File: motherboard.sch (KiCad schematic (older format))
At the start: 90 parts, among them P1 CONN_01X08, P2 CONN_01X08, P3 CONN_01X29, P4 CONN_01X25, U1 STM32F411-LQFP64, U10 74LS125, U11 74LS125, U12 74LS125, U13 74LS125, U14 74LS125, U15 PCA9517A, U16 PCA9517A, U2 STM32F411-LQFP64, U3 AP7313, U4 74LVC2G132, U5 FM25V20A-G, U6 FM25V20A-G, U7 FM25V20A-G, U8 FM25V20A-G, U9 74LS125, Y1 32k, Y2 8M(16pF), Y3 32k, Y4 8M(16pF)

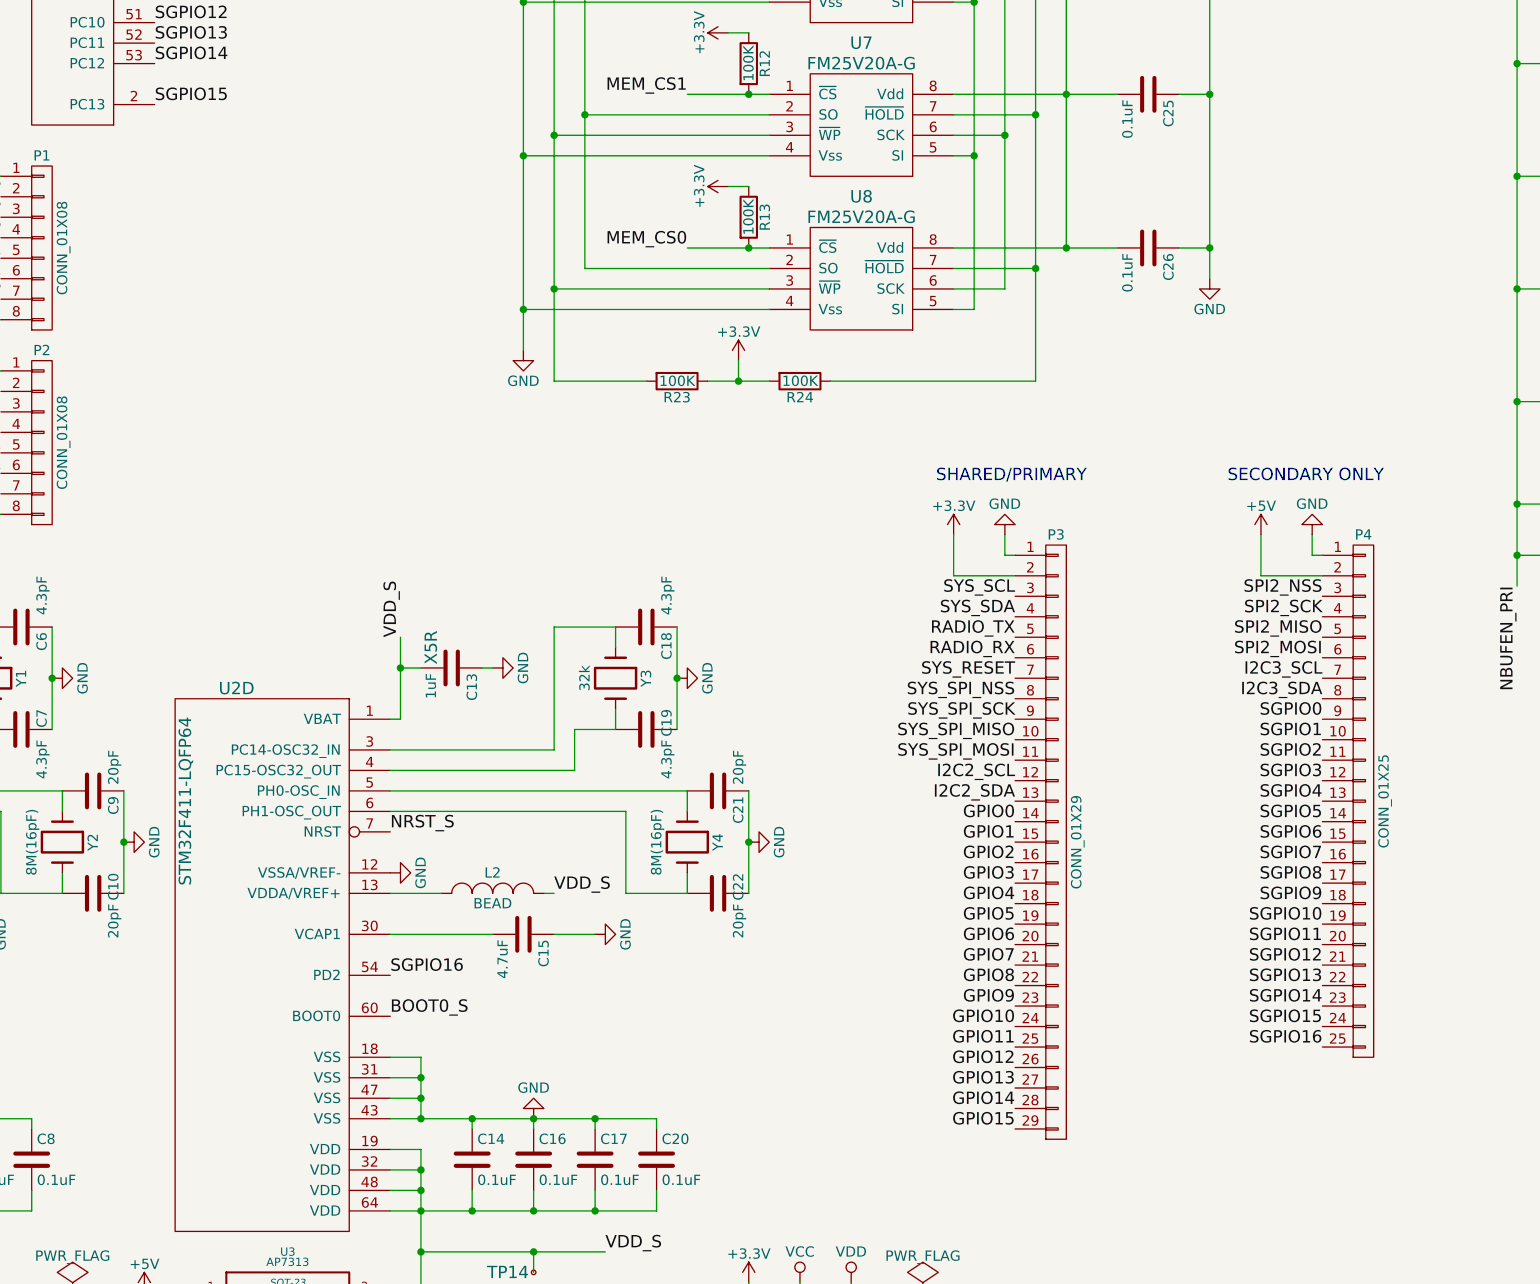
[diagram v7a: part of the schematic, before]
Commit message: Began adding real connectors to schematic
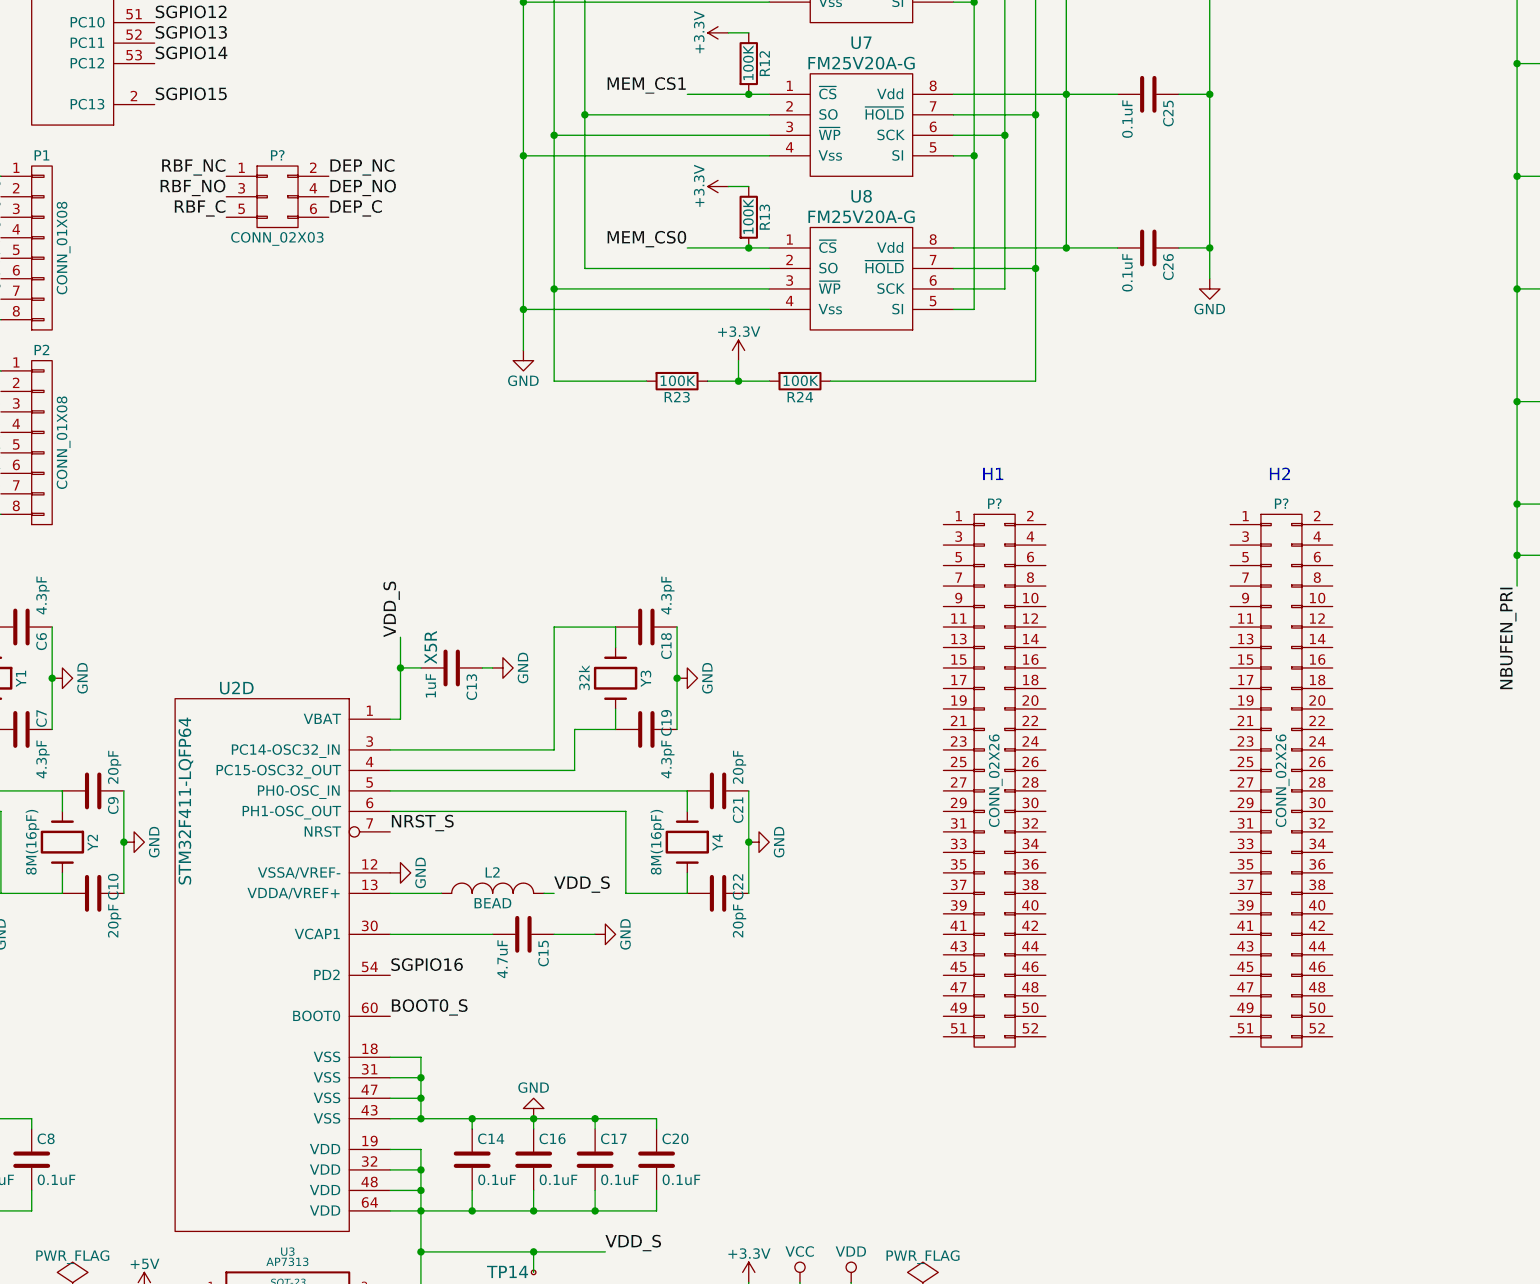
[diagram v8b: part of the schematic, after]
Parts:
- removed P3: CONN_01X29, symbol CONN_01X29
- removed P4: CONN_01X25, symbol CONN_01X25
- added P?: CONN_02X03, symbol CONN_02X03
- added P? (x2): CONN_02X26, symbol CONN_02X26
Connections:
- new net DEP_C: P?.6 (P6)
- new net DEP_NC: P?.2 (P2)
- new net DEP_NO: P?.4 (P4)
- new net RBF_C: P?.5 (P5)
- new net RBF_NC: P?.1 (P1)
- new net RBF_NO: P?.3 (P3)
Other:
- note added: "H1"
- note added: "H2"
- note removed: "SECONDARY ONLY"
- note removed: "SHARED/PRIMARY"
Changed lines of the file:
@@
 	6000 10400 6000 10500
 Connection ~ 6000 10400
-Wire Wire Line
-	8050 7100 8350 7100
-Wire Wire Line
-	8050 7100 8050 6900
-Wire Wire Line
-	8350 7000 8300 7000
-Wire Wire Line
-	8300 7000 8300 6900
-$Comp
-L +3.3V #PWR041
-U 1 1 56F839C7
-P 8050 6900
-F 0 "#PWR041" H 8050 6750 50  0001 C CNN
-F 1 "+3.3V" H 8050 7040 50  0000 C CNN
-F 2 "" H 8050 6900 60  0000 C CNN
-F 3 "" H 8050 6900 60  0000 C CNN
-	1    8050 6900
-	1    0    0    -1
-$EndComp
-$Comp
-L GND #PWR042
-U 1 1 56F83D7F
-P 8300 6900
-F 0 "#PWR042" H 8300 6650 50  0001 C CNN
-F 1 "GND" H 8300 6750 50  0000 C CNN
-F 2 "" H 8300 6900 60  0000 C CNN
-F 3 "" H 8300 6900 60  0000 C CNN
-	1    8300 6900
-	-1   0    0    1
-$EndComp
-Text Label 8350 7300 2    60   ~ 0
-SYS_SDA
-Text Label 8350 7200 2    60   ~ 0
-SYS_SCL
-Text Label 8350 7400 2    60   ~ 0
-RADIO_TX
-Text Label 8350 7500 2    60   ~ 0
-RADIO_RX
 Text Label 1450 2050 0    60   ~ 0
 SYS_RESET_P
 Text Label 1450 4300 0    60   ~ 0
 SYS_RESET_S
-Text Label 8350 7600 2    60   ~ 0
-SYS_RESET
-Text Label 8350 7700 2    60   ~ 0
-SYS_SPI_NSS
-Text Label 8350 7800 2    60   ~ 0
-SYS_SPI_SCK
-Text Label 8350 7900 2    60   ~ 0
-SYS_SPI_MISO
-Text Label 8350 8000 2    60   ~ 0
-SYS_SPI_MOSI
-Text Label 9850 7200 2    60   ~ 0
-SPI2_NSS
-Text Label 9850 7300 2    60   ~ 0
-SPI2_SCK
-Text Label 9850 7400 2    60   ~ 0
-SPI2_MISO
-Text Label 9850 7500 2    60   ~ 0
-SPI2_MOSI
-Text Label 8350 8400 2    60   ~ 0
-GPIO1
-Text Label 8350 8500 2    60   ~ 0
-GPIO2
-Text Label 8350 8600 2    60   ~ 0
-GPIO3
-Text Label 8350 8700 2    60   ~ 0
-GPIO4
-Text Label 8350 8800 2    60   ~ 0
-GPIO5
-Text Label 8350 8900 2    60   ~ 0
-GPIO6
-Text Label 8350 9000 2    60   ~ 0
-GPIO7
 Text Label 2800 1100 0    60   ~ 0
 I2C2_SCL
@@
 Text Label 2800 4750 0    60   ~ 0
 I2C3_SDA
-Text Label 8350 8200 2    60   ~ 0
-I2C2_SDA
-Text Label 8350 8100 2    60   ~ 0
-I2C2_SCL
-Text Label 8350 8300 2    60   ~ 0
-GPIO0
-Text Label 8350 9300 2    60   ~ 0
-GPIO10
-Text Label 8350 9400 2    60   ~ 0
-GPIO11
-Text Label 8350 9500 2    60   ~ 0
-GPIO12
-Text Label 8350 9600 2    60   ~ 0
-GPIO13
-Text Label 8350 9700 2    60   ~ 0
-GPIO14
-Text Label 8350 9800 2    60   ~ 0
-GPIO15
-Text Label 8350 9200 2    60   ~ 0
-GPIO9
-Text Label 8350 9100 2    60   ~ 0
-GPIO8
-Text Notes 8700 6650 2    60   ~ 0
-SHARED/PRIMARY
-Text Notes 10150 6650 2    60   ~ 0
-SECONDARY ONLY
-Wire Wire Line
-	9550 7100 9850 7100
-Wire Wire Line
-	9550 7100 9550 6900
-Wire Wire Line
-	9850 7000 9800 7000
-Wire Wire Line
-	9800 7000 9800 6900
-$Comp
-L GND #PWR043
-U 1 1 56FAD746
-P 9800 6900
-F 0 "#PWR043" H 9800 6650 50  0001 C CNN
-F 1 "GND" H 9800 6750 50  0000 C CNN
-F 2 "" H 9800 6900 60  0000 C CNN
-F 3 "" H 9800 6900 60  0000 C CNN
-	1    9800 6900
-	-1   0    0    1
-$EndComp
-Text Label 9850 7600 2    60   ~ 0
-I2C3_SCL
-Text Label 9850 7700 2    60   ~ 0
-I2C3_SDA
-Text Label 9850 7900 2    60   ~ 0
-SGPIO1
-Text Label 9850 8000 2    60   ~ 0
-SGPIO2
-Text Label 9850 8100 2    60   ~ 0
-SGPIO3
-Text Label 9850 8200 2    60   ~ 0
-SGPIO4
-Text Label 9850 8300 2    60   ~ 0
-SGPIO5
-Text Label 9850 8400 2    60   ~ 0
-SGPIO6
-Text Label 9850 8500 2    60   ~ 0
-SGPIO7
-Text Label 9850 7800 2    60   ~ 0
-SGPIO0
-Text Label 9850 8800 2    60   ~ 0
-SGPIO10
-Text Label 9850 8900 2    60   ~ 0
-SGPIO11
-Text Label 9850 9000 2    60   ~ 0
-SGPIO12
-Text Label 9850 9100 2    60   ~ 0
-SGPIO13
-Text Label 9850 9200 2    60   ~ 0
-SGPIO14
-Text Label 9850 9300 2    60   ~ 0
-SGPIO15
-Text Label 9850 8700 2    60   ~ 0
-SGPIO9
-Text Label 9850 8600 2    60   ~ 0
-SGPIO8
-Text Label 9850 9400 2    60   ~ 0
-SGPIO16
+Text Notes 8300 6650 2    60   ~ 0
+H1
 Text Label 1450 750  0    60   ~ 0
 GPIO0
@@
 	1    0    0    -1
 $EndComp
-$Comp
-L +5V #PWR045
-U 1 1 56FC29CE
-P 9550 6900
-F 0 "#PWR045" H 9550 6750 50  0001 C CNN
-F 1 "+5V" H 9550 7040 50  0000 C CNN
-F 2 "" H 9550 6900 60  0000 C CNN
-F 3 "" H 9550 6900 60  0000 C CNN
-	1    9550 6900
-	1    0    0    -1
-$EndComp
 Wire Wire Line
 	13350 8900 13400 8900
@@
 Text Label 2800 4250 0    60   ~ 0
 MEM_NHOLD_S
-$Comp
-L CONN_01X29 P3
-U 1 1 56FE86BF
-P 8550 8400
-F 0 "P3" H 8550 9900 50  0000 C CNN
-F 1 "CONN_01X29" V 8650 8400 50  0000 C CNN
-F 2 "" H 8550 8400 60  0000 C CNN
-F 3 "" H 8550 8400 60  0000 C CNN
-	1    8550 8400
-	1    0    0    -1
-$EndComp
-$Comp
-L CONN_01X25 P4
-U 1 1 56FE90B2
-P 10050 8200
-F 0 "P4" H 10050 9500 50  0000 C CNN
-F 1 "CONN_01X25" V 10150 8200 50  0000 C CNN
-F 2 "" H 10050 8200 60  0000 C CNN
-F 3 "" H 10050 8200 60  0000 C CNN
-	1    10050 8200
-	1    0    0    -1
-$EndComp
 Text Label 4150 800  0    60   ~ 0
 GPIO3
@@
 Connection ~ 2900 5850
 Connection ~ 2900 6100
+$Comp
+L CONN_02X03 P?
+U 1 1 581E4EE0
+P 4750 5250
+F 0 "P?" H 4750 5450 50  0000 C CNN
+F 1 "CONN_02X03" H 4750 5050 50  0000 C CNN
+F 2 "" H 4750 4050 50  0000 C CNN
+F 3 "" H 4750 4050 50  0000 C CNN
+	1    4750 5250
+	1    0    0    -1
+$EndComp
+Text Label 4500 5150 2    60   ~ 0
+RBF_NC
+Text Label 4500 5250 2    60   ~ 0
+RBF_NO
+Text Label 4500 5350 2    60   ~ 0
+RBF_C
+Text Label 5000 5150 0    60   ~ 0
+DEP_NC
+Text Label 5000 5250 0    60   ~ 0
+DEP_NO
+Text Label 5000 5350 0    60   ~ 0
+DEP_C
+$Comp
+L CONN_02X26 P?
+U 1 1 581EA932
+P 8250 8100
+F 0 "P?" H 8250 9450 50  0000 C CNN
+F 1 "CONN_02X26" V 8250 8100 50  0000 C CNN
+F 2 "" H 8250 7400 50  0000 C CNN
+F 3 "" H 8250 7400 50  0000 C CNN
+	1    8250 8100
+	1    0    0    -1
+$EndComp
+Text Notes 9700 6650 2    60   ~ 0
+H2
+$Comp
+L CONN_02X26 P?
+U 1 1 581EB706
+P 9650 8100
+F 0 "P?" H 9650 9450 50  0000 C CNN
+F 1 "CONN_02X26" V 9650 8100 50  0000 C CNN
+F 2 "" H 9650 7400 50  0000 C CNN
+F 3 "" H 9650 7400 50  0000 C CNN
+	1    9650 8100
+	1    0    0    -1
+$EndComp
 $EndSCHEMATC
